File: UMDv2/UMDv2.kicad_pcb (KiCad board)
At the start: 2 copper layers, 104.1 x 83.8 mm, 107 parts, among them CON201 10118194-0001LF, CON301 USB-B1HSB6, CON302 JTAG-2X10-HDR, CON303 101-00405-75, CON304 UMDv2-CONN, CON305 HDR1X2, CON306 HDR1X3, Q201 SMMBT3904LT1G, SW301 PTS645SM43SMTR92_LFS, SW302 PTS645SM43SMTR92_LFS, U201 MIC5504-3.3YM5-TR, U202 TPS2115APWR, U203 AP22802BW5-7, U204 AP22802BW5-7, U205 AZ1117CH-3.3TRG1, U206 AP22802BW5-7, U207 INA199A2DCKR, U301 STM32F407ZET6, U302 74ALVC164245DL,118, U303 74ALVC164245DL,118, U305 S25FL127SABMFI101, X301 ECS-80-18-30-JGN-TR

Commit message: routing the PCB
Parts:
- added R312: 0, db-smt:0603, F.Cu at (119.8, 94.7)
- moved R309 59.3 mm to (127.8, 113.2)
- moved R310 58.4 mm to (127.8, 114.9)
- moved C305 11.1 mm to (135.5, 96.6)
- moved C301 9.95 mm to (114.7, 80.9), turned to 180 degrees
- moved D301 9.89 mm to (113.6, 82.7)
- moved D302 4.97 mm to (167.7, 119.0)
- moved C202 4.26 mm to (116.3, 86.8)
- moved D304 4.26 mm to (112.9, 92.8)
- moved F301 4.26 mm to (112.8, 89.6)
- moved R305 4.26 mm to (115.9, 92.8)
- moved TP203 4.26 mm to (127.4, 91.4)
- moved U201 4.26 mm to (120.6, 88.8)
- moved C205 4.26 mm to (123.3, 91.3)
- moved D303 3.83 mm to (171.7, 118.9), turned to 0 degrees
- moved C217 3.83 mm to (151.1, 113.6), turned to 0 degrees
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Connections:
- CON304 pad 17: /Microcontroller/D1 -> /Microcontroller/D12
- CON304 pad 18: /Microcontroller/D11 -> /Microcontroller/D10
- CON304 pad 19: /Microcontroller/D9 -> /Microcontroller/D8
- CON304 pad 20: /Microcontroller/D7 -> /Microcontroller/D6
- CON304 pad 21: /Microcontroller/D5 -> /Microcontroller/D4
- CON304 pad 44: /Microcontroller/D4 -> /Microcontroller/D5
- CON304 pad 45: /Microcontroller/D6 -> /Microcontroller/D7
- CON304 pad 46: /Microcontroller/D8 -> /Microcontroller/D9
- CON304 pad 47: /Microcontroller/D10 -> /Microcontroller/D11
- CON304 pad 48: /Microcontroller/D12 -> /Microcontroller/D3
- CON304 pad 49: /Microcontroller/D3 -> /Microcontroller/D0
- CON304 pad 50: /Microcontroller/D0 -> /Microcontroller/D14
- CON304 pad 51: /Microcontroller/D14 -> /Microcontroller/D1
- U301 pad 101: /Microcontroller/Vbus -> Net-(R312-Pad2)
- U301 pad 132: Net-(U301-Pad132) -> /Microcontroller/~SDCD~
- U301 pad 37: /Microcontroller/~OUT_EN~ -> /Microcontroller/~OUT_EN0~
- U301 pad 49: Net-(U301-Pad49) -> /Microcontroller/~OUT_EN1~
- U301 pad 7: /Microcontroller/~SDCD~ -> Net-(U301-Pad7)
- U302 pad 25: /Microcontroller/~OUT_EN~ -> /Microcontroller/~OUT_EN1~
- U302 pad 48: /Microcontroller/~OUT_EN~ -> /Microcontroller/~OUT_EN1~
- U303 pad 25: /Microcontroller/~OUT_EN~ -> /Microcontroller/~OUT_EN0~
- U303 pad 48: /Microcontroller/~OUT_EN~ -> /Microcontroller/~OUT_EN0~
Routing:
- net +3.3VP: track 116.2 -> 164.6 mm, vias 10 -> 12
- net /Microcontroller/D5: track 0.00 -> 44.0 mm
- net /Microcontroller/D7: track 0.00 -> 43.7 mm
- net /Microcontroller/GP0: track 0.00 -> 43.3 mm
- net /Microcontroller/D9: track 0.00 -> 43.1 mm
- net /Microcontroller/GP1: track 0.00 -> 42.5 mm
- net /Microcontroller/D11: track 0.00 -> 42.4 mm
- net /Microcontroller/SDIO_D2: track 0.00 -> 30.3 mm
- net /Microcontroller/D4: track 0.00 -> 28.7 mm
- net /Microcontroller/D6: track 0.00 -> 27.8 mm
- net /Microcontroller/D8: track 0.00 -> 27.6 mm
- net /Microcontroller/SEL1: track 0.00 -> 27.2 mm
- net /Microcontroller/D10: track 0.00 -> 27.0 mm
- net /Microcontroller/SDIO_D3: track 0.00 -> 26.8 mm
- net /Microcontroller/SEL0: track 0.00 -> 26.5 mm
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
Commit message: more routing
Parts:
- moved C220 0.31 mm to (171.3, 102.2)
- moved C219 0.31 mm to (171.3, 84.1)
- moved C224 0.27 mm to (171.4, 140.2)
- moved C223 0.26 mm to (171.4, 121.9)
- moved C222 0.25 mm to (165.8, 84.2)
- moved C225 0.23 mm to (165.8, 140.2)
- moved C226 0.20 mm to (165.8, 121.9)
- moved C221 0.18 mm to (165.8, 102.2)
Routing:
- net GND: track 65.3 -> 184.4 mm, vias 23 -> 45
- net VDD: track 64.9 -> 152.4 mm, vias 0 -> 2
- net +3V3: track 75.8 -> 158.8 mm, vias 2 -> 4
- net /Microcontroller/~CE2~: track 0.00 -> 70.3 mm, vias 0 -> 4
- net /Microcontroller/~CE1~: track 0.00 -> 69.1 mm, vias 0 -> 4
- net /Microcontroller/~CE0~: track 0.00 -> 68.8 mm, vias 0 -> 4
- net /Microcontroller/~CE3~: track 0.00 -> 68.0 mm, vias 0 -> 4
- net /Microcontroller/A6: track 0.00 -> 22.2 mm, vias 0 -> 2
- net +3.3VP: track 164.6 -> 178.7 mm
- net /Microcontroller/~SDCD~: track 15.8 -> 28.9 mm
- net /Microcontroller/~OUT_EN0~: track 0.00 -> 11.3 mm, vias 0 -> 2
- net /Microcontroller/A0: track 39.4 -> 36.8 mm
- net /Microcontroller/A22: track 40.8 -> 38.2 mm
- net /Microcontroller/A1: track 39.1 -> 36.5 mm
- net /Microcontroller/A21: track 41.0 -> 38.5 mm
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
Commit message: lots of routing work
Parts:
- moved C310 17.9 mm to (174.6, 67.1), turned to 0 degrees
- moved CON306 11.1 mm to (156.8, 93.2), turned to 0 degrees
- moved C313 2.74 mm to (159.6, 102.0)
- moved C311 0.80 mm to (192.5, 140.6)
- moved C309 0.55 mm to (175.7, 64.4), turned to 0 degrees
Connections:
- CON304 pad 14: /Microcontroller/D13 -> /Microcontroller/D0
- CON304 pad 15: /Microcontroller/D15 -> /Microcontroller/D14
- CON304 pad 49: /Microcontroller/D0 -> /Microcontroller/D13
- CON304 pad 50: /Microcontroller/D14 -> /Microcontroller/D15
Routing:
- net Vcart: track 34.7 -> 129.1 mm, vias 2 -> 3
- net /Microcontroller/D3: track 0.00 -> 82.3 mm, vias 0 -> 2
- net /Microcontroller/D2: track 0.00 -> 67.4 mm, vias 0 -> 2
- net /Microcontroller/D1: track 0.00 -> 58.9 mm, vias 0 -> 4
- net /Microcontroller/D15: track 0.00 -> 57.3 mm, vias 0 -> 2
- net /Microcontroller/~RD~: track 0.00 -> 54.6 mm, vias 0 -> 2
- net /Microcontroller/~WR~: track 0.00 -> 53.9 mm, vias 0 -> 2
- net /Microcontroller/D13: track 0.00 -> 50.8 mm, vias 0 -> 2
- net /Microcontroller/SDA1: track 4.78 -> 49.3 mm, vias 0 -> 1
- net /Microcontroller/SCL1: track 5.33 -> 48.0 mm, vias 0 -> 1
- net /Microcontroller/JTMS: track 1.83 -> 42.8 mm
- net /Microcontroller/D0: track 0.00 -> 39.8 mm, vias 0 -> 3
- net /Microcontroller/JTCK: track 0.00 -> 37.1 mm, vias 0 -> 1
- net /Microcontroller/D14: track 0.00 -> 36.7 mm, vias 0 -> 1
- net /Microcontroller/JTDI: track 0.00 -> 32.0 mm, vias 0 -> 1
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
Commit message: the time they are a-routing
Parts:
- CON302: footprint db-thparts:HDR2X10-JTAG -> db-thparts:HDR2X10-JTAG-SHROUD
- moved C308 31.7 mm to (137.4, 134.7)
- moved R304 23.7 mm to (123.8, 133.5)
- moved R303 21.1 mm to (121.2, 133.5), turned to 90 degrees
- moved R310 19.9 mm to (127.2, 95.0), turned to 270 degrees
- moved C304 19.4 mm to (118.6, 133.5)
- moved R309 18.4 mm to (125.4, 95.0), turned to 270 degrees
- moved R307 12.1 mm to (125.2, 129.2)
- moved D305 8.81 mm to (125.5, 125.5), turned to 90 degrees
- moved R311 6.76 mm to (119.3, 127.4), turned to 90 degrees
- moved CON305 6.50 mm to (115.9, 127.4)
- moved CON302 3.18 mm to (141.6, 138.8)
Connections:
- D305 pad 2: /Microcontroller/BOOT_LED -> /Microcontroller/STAT_LED
- U301 pad 139: Net-(U301-Pad139) -> /Microcontroller/STAT_LED
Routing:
- net +3.3VP: track 181.5 -> 245.4 mm, vias 13 -> 14
- net /Microcontroller/~RST: track 0.00 -> 43.5 mm, vias 0 -> 3
- net /Microcontroller/JTDO: track 0.00 -> 31.9 mm, vias 0 -> 1
- net /Microcontroller/JRST: track 0.00 -> 31.2 mm, vias 0 -> 1
- net Net-(C304-Pad1): track 0.00 -> 29.2 mm
- net /Microcontroller/BOOT0: track 0.00 -> 18.6 mm
- net /Microcontroller/JTDI: track 32.0 -> 42.2 mm
- net /Microcontroller/JTMS: track 42.8 -> 49.5 mm
- net /Microcontroller/JTCK: track 37.1 -> 42.3 mm
- net /Microcontroller/SCL1: track 48.0 -> 50.0 mm
- net /Microcontroller/SDA1: track 49.3 -> 51.1 mm

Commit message: routing
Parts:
- added D306: LO_M67K-K2M1-24-Z, db-smt:SMD-2, F.Cu at (127.4, 124.9)
- added R313: 750, db-smt:0603, F.Cu at (127.4, 127.4)
- moved R307 5.77 mm to (130.7, 127.5), turned to 90 degrees
- moved D305 5.16 mm to (130.6, 124.9)
- moved C313 0.29 mm to (159.5, 101.7)
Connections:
- D305 pad 2: /Microcontroller/STAT_LED -> /Microcontroller/LED0
- U301 pad 135: Net-(U301-Pad135) -> /Microcontroller/PRG_BTN
- U301 pad 139: /Microcontroller/STAT_LED -> /Microcontroller/LED1
- U301 pad 140: Net-(U301-Pad140) -> /Microcontroller/LED0
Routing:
- net /Microcontroller/iSense: track 8.24 -> 66.7 mm, vias 1 -> 4
- net /Microcontroller/PRG_BTN: track 0.00 -> 52.3 mm, vias 0 -> 2
- net /Microcontroller/SPI2_MISO: track 14.0 -> 61.6 mm, vias 1 -> 2
- net GND: track 186.4 -> 140.8 mm, vias 45 -> 390
- net /Microcontroller/SPI2_NSS: track 14.7 -> 60.3 mm, vias 1 -> 2
- net /Microcontroller/GP6: track 26.9 -> 70.1 mm, vias 0 -> 2
- net /Microcontroller/SDA1: track 51.1 -> 91.7 mm
- net /Microcontroller/SCL1: track 50.0 -> 89.5 mm
- net /Microcontroller/SPI2_MOSI: track 13.8 -> 46.5 mm
- net /Microcontroller/SPI2_SCK: track 14.4 -> 45.2 mm
- net /Microcontroller/~SDCD~: track 27.9 -> 54.9 mm, vias 0 -> 2
- net +3.3VP: track 245.4 -> 258.8 mm
- net /Microcontroller/LED1: track 0.00 -> 10.6 mm
- net /Microcontroller/LED0: track 0.00 -> 8.21 mm
- net /Microcontroller/~RST: track 43.5 -> 36.0 mm, vias 3 -> 2
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- added copper zone on B.Cu, net GND
- added copper zone on F.Cu, net GND

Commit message: just a-routing
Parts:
- U203, U204, U206: value AP22802BW5-7 -> AP22802AW5-7
- moved C313 2.58 mm to (157.0, 101.4), turned to 0 degrees
- moved R310 1.88 mm to (125.3, 95.0)
- moved R309 1.57 mm to (126.9, 95.0)
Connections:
- CON306 pad 2: /Microcontroller/USART3_TX -> /Microcontroller/USART3_RX
- CON306 pad 3: /Microcontroller/USART3_RX -> /Microcontroller/USART3_TX
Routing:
- net Vcart: track 129.1 -> 136.2 mm
- net GND: track 140.8 -> 135.0 mm, vias 390 -> 384
- net /Microcontroller/SDA1: track 91.7 -> 95.6 mm, vias 1 -> 2
- net /Microcontroller/USART3_RX: track 8.28 -> 11.9 mm
- net /Microcontroller/USART3_TX: track 13.3 -> 9.70 mm
- net /Microcontroller/D14: track 36.7 -> 40.2 mm
- net /Microcontroller/SCL1: track 89.5 -> 92.7 mm, vias 1 -> 2
- net Net-(C313-Pad1): track 5.12 -> 2.63 mm
- net /Microcontroller/D15: track 57.3 -> 55.3 mm
- net /Microcontroller/D13: track 50.8 -> 52.2 mm

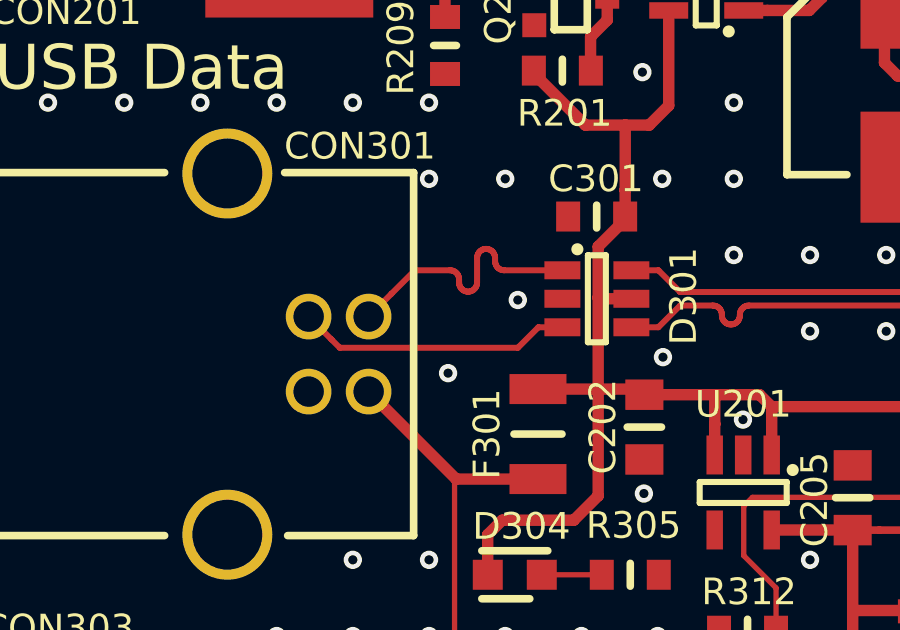
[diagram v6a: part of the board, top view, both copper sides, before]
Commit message: added 1.5k pullep to USB D+
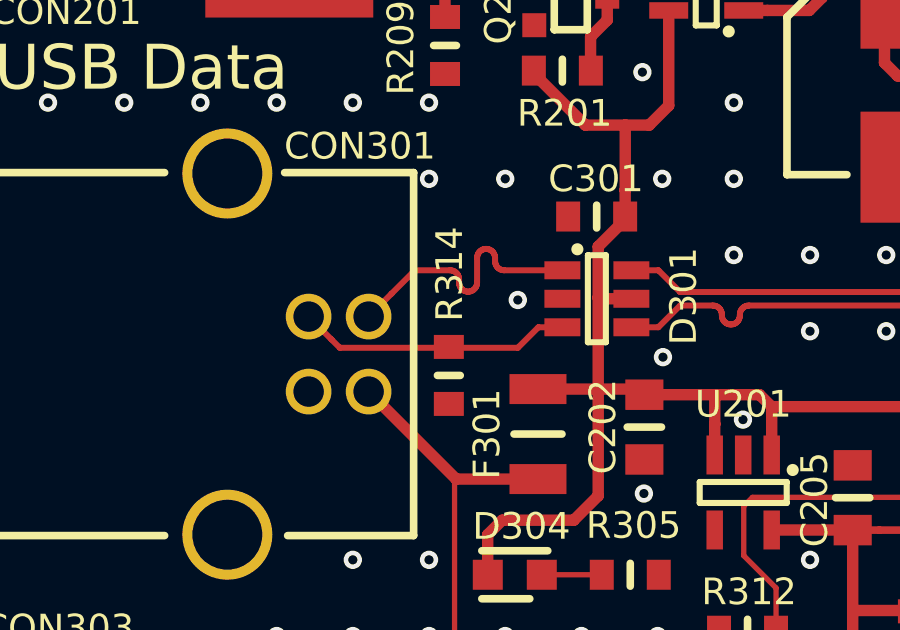
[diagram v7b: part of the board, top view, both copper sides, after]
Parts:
- added R314: 1.50k, db-smt:0603, F.Cu at (109.8, 86.2)
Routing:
- net GND: vias 384 -> 383
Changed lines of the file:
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@@
     (thickness 1.6)
     (drawings 19)
-    (tracks 2193)
+    (tracks 2192)
     (zones 0)
-    (modules 110)
+    (modules 111)
     (nets 187)
   )
@@
   )
   (module db-smt:0603 (layer F.Cu)
+    (at 109.8169 86.1568 90)
+    (tags 0603)
+    (solder_mask_margin 0.1016)
+    (attr smd)
+    (fp_text reference R314 (at 3.3782 0.0254 90) (layer F.SilkS)
+      (effects (font (size 0.889 0.889) (thickness 0.2032)))
+    )
+    (fp_text value 1.50k (at 0.508 -2.54 90) (layer F.Fab) hide
+      (effects (font (size 1 1) (thickness 0.15)))
+    )
+    (fp_line (start 0 -0.381) (end 0 0.381) (layer F.SilkS) (width 0.254))
+    (pad 1 smd rect (at -0.95 0 90) (size 0.8 1) (layers F.Cu F.Paste F.Mask)
+      (net 6 +3.3VP))
+    (pad 2 smd rect (at 0.95 0 90) (size 0.8 1) (layers F.Cu F.Paste F.Mask)
+      (net 103 /Microcontroller/Din+))
+    (model Resistors_SMD.3dshapes/R_0603.wrl
+      (at (xyz 0 0 0))
+      (scale (xyz 1 1 1))
+      (rotate (xyz 0 0 0))
+    )
+  )
+  (module db-smt:0603 (layer F.Cu)
     (at 127.4445 127.4318 90)
     (tags 0603)
@@
   (via (at 99.5045 71.4756) (size 0.6096) (drill 0.3048) (layers F.Cu B.Cu) (net 1))
   (via (at 99.5045 69.4436) (size 0.6096) (drill 0.3048) (layers F.Cu B.Cu) (net 1))
-  (via (at 109.7915 86.0806) (size 0.6096) (drill 0.3048) (layers F.Cu B.Cu) (net 1))
   (via (at 139.1285 105.1052) (size 0.6096) (drill 0.3048) (layers F.Cu B.Cu) (net 1))
   (via (at 139.1285 107.5436) (size 0.6096) (drill 0.3048) (layers F.Cu B.Cu) (net 1))
@@
     (connect_pads (clearance 0.1778))
     (min_thickness 0.1778)
-    (fill yes (arc_segments 32) (thermal_gap 0.254) (thermal_bridge_width 0.254) (smoothing fillet))
+    (fill (arc_segments 32) (thermal_gap 0.254) (thermal_bridge_width 0.254) (smoothing fillet))
     (polygon
       (pts
@@
     (connect_pads (clearance 0.1778))
     (min_thickness 0.1778)
-    (fill yes (arc_segments 32) (thermal_gap 0.254) (thermal_bridge_width 0.254) (smoothing fillet))
+    (fill (arc_segments 32) (thermal_gap 0.254) (thermal_bridge_width 0.254) (smoothing fillet))
     (polygon
       (pts

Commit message: changed MCU to STM32F413
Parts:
- U301: value STM32F407ZET6 -> STM32F413ZHT6
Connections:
- U301 pad 126: Net-(U301-Pad126) -> /Microcontroller/GP6
- U301 pad 40: /Microcontroller/SPI1_NSS -> Net-(U301-Pad40)
- U301 pad 41: /Microcontroller/SPI1_SCK -> Net-(U301-Pad41)
- U301 pad 42: /Microcontroller/SPI1_MISO -> Net-(U301-Pad42)
- U301 pad 43: /Microcontroller/SPI1_MOSI -> Net-(U301-Pad43)
- U301 pad 91: /Microcontroller/SEL0 -> Net-(U301-Pad91)
- U301 pad 92: /Microcontroller/SEL1 -> /Microcontroller/SEL0
- U301 pad 93: /Microcontroller/GP6 -> /Microcontroller/SEL1
